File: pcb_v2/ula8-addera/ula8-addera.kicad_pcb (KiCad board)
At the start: 2 copper layers, 54.4 x 61 mm, 13 parts, among them J1 ula8a, U1 74LS283, U2 74LS283, U3 74LS244, U4 74LS125

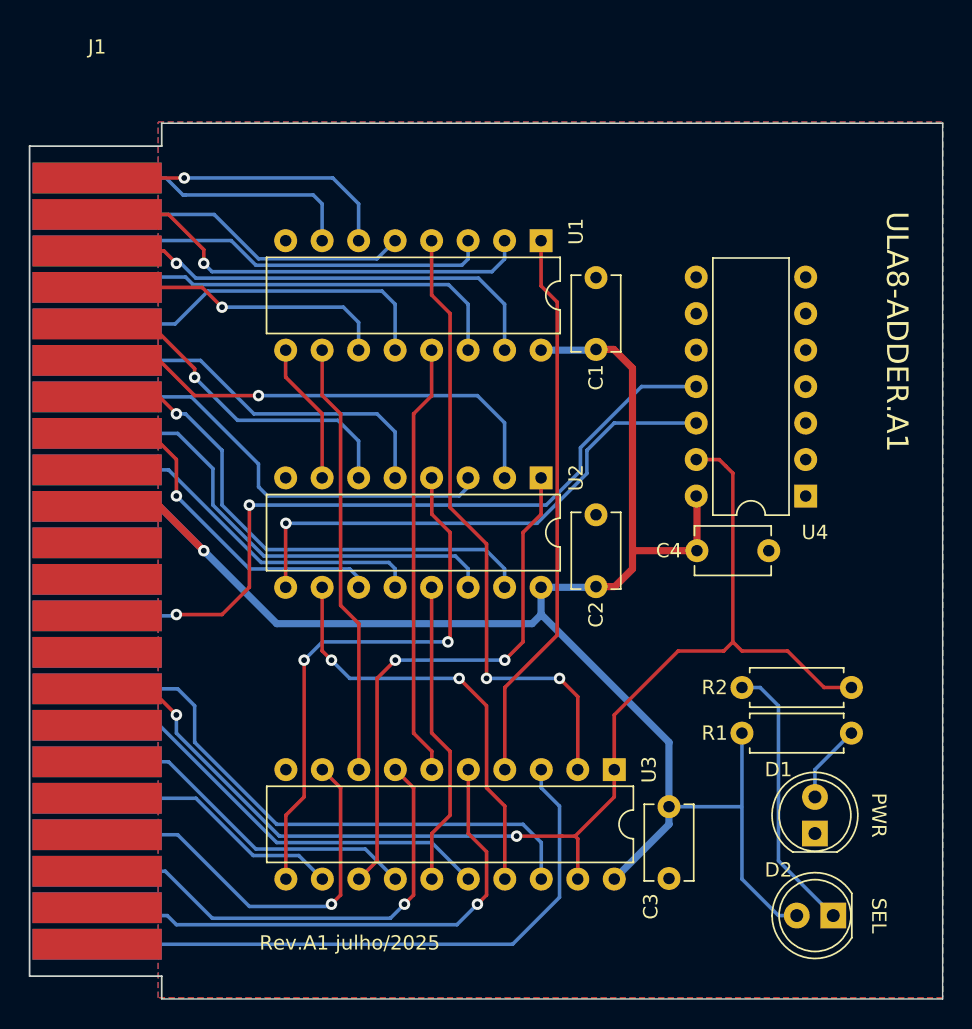
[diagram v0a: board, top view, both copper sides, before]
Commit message: vias de alimentacao movidas para as extremidades do conector
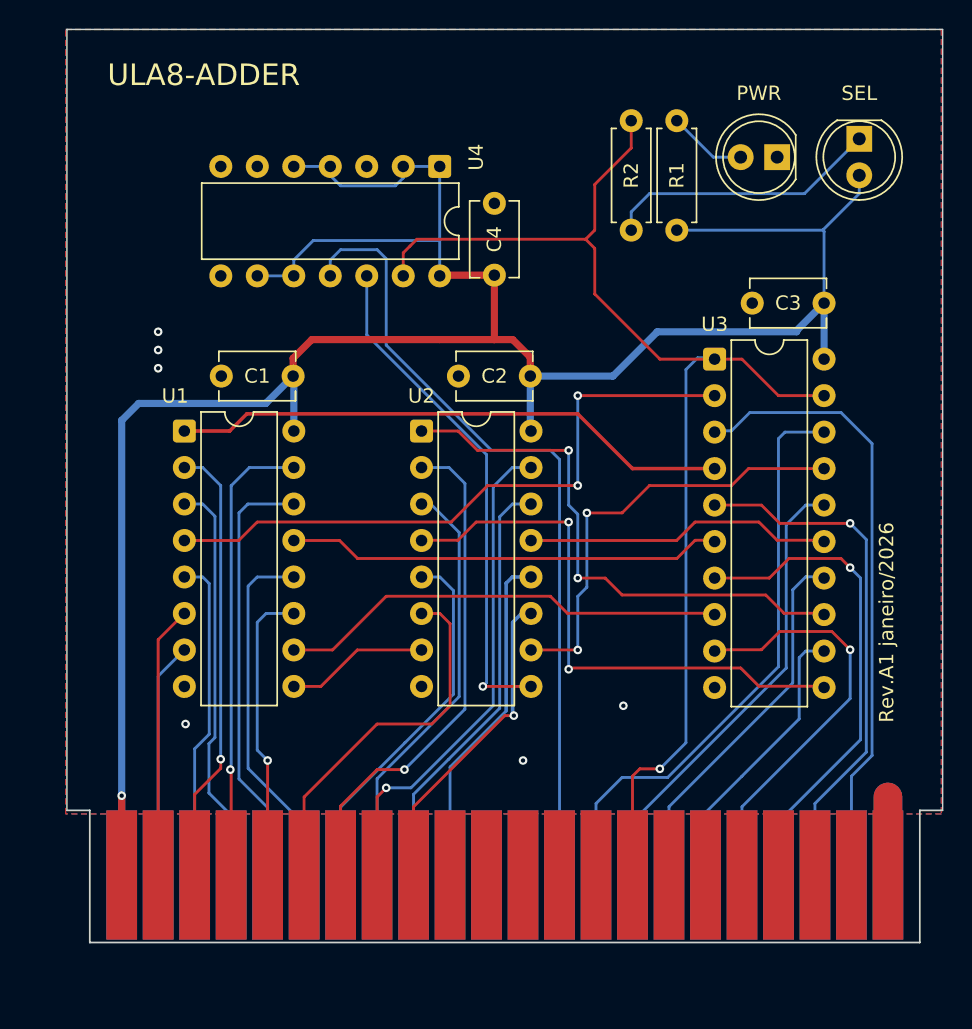
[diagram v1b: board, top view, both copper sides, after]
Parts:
- moved D2 54.1 mm to (83.1, 27.2), turned to -90 degrees
- moved J1 48.6 mm to (31.8, 78.5), turned to 90 degrees
- moved D1 47.2 mm to (77.4, 28.5), turned to 180 degrees
- moved C3 40.5 mm to (75.6, 38.6), turned to 0 degrees
- moved R1 35.3 mm to (70.4, 33.6), turned to 90 degrees
- moved U4 34.3 mm to (53.9, 29.1), turned to -90 degrees
- moved R2 32.8 mm to (67.2, 33.6), turned to 90 degrees
- moved U3 29.4 mm to (73.0, 42.5), turned to 0 degrees
- moved U1 28.1 mm to (36.1, 47.5), turned to 0 degrees
- moved C1 27.0 mm to (38.7, 43.7), turned to 0 degrees
- moved C4 23.8 mm to (57.7, 36.7), turned to 90 degrees
- moved C2 13.6 mm to (55.2, 43.7), turned to 0 degrees
- moved U2 8.94 mm to (52.6, 47.5), turned to 0 degrees
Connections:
- net n_select renamed ~{select}
- J1 pad 1: lower_bus0 -> +5V
- J1 pad 10: +5V -> unconnected-(J1-Pin_10-Pad10)
- J1 pad 11: GND -> unconnected-(J1-Pin_11-Pad11)
- J1 pad 2: lower_bus1 -> lower_bus0
- J1 pad 22: unconnected-(J1-Pad22) -> GND
- J1 pad 23: carry_in -> +5V
- J1 pad 24: upper_bus0 -> carry_in
- J1 pad 25: upper_bus1 -> upper_bus0
- J1 pad 26: upper_bus2 -> upper_bus1
- J1 pad 27: upper_bus3 -> upper_bus2
- J1 pad 28: upper_bus4 -> upper_bus3
- J1 pad 29: upper_bus5 -> upper_bus4
- J1 pad 3: lower_bus2 -> lower_bus1
- J1 pad 30: upper_bus6 -> upper_bus5
- J1 pad 31: upper_bus7 -> upper_bus6
- J1 pad 32: +5V -> upper_bus7
- J1 pad 33: GND -> unconnected-(J1-Pin_33-Pad33)
- J1 pad 36: unconnected-(J1-Pad36) -> ula_bus0
- J1 pad 37: ula_bus0 -> ula_bus1
- J1 pad 38: ula_bus1 -> ula_bus2
- J1 pad 39: ula_bus2 -> ula_bus3
- J1 pad 4: lower_bus3 -> lower_bus2
- J1 pad 40: ula_bus3 -> ula_bus4
- J1 pad 41: ula_bus4 -> ula_bus5
- J1 pad 42: ula_bus5 -> ula_bus6
- J1 pad 43: ula_bus6 -> ula_bus7
- J1 pad 44: ula_bus7 -> GND
- J1 pad 5: lower_bus4 -> lower_bus3
- J1 pad 6: lower_bus5 -> lower_bus4
- J1 pad 7: lower_bus6 -> lower_bus5
- J1 pad 8: lower_bus7 -> lower_bus6
- J1 pad 9: unconnected-(J1-Pad9) -> lower_bus7
- U4 pad 1: unconnected-(U4-Pad1) -> +5V
- U4 pad 10: unconnected-(U4-Pad10) -> +5V
- U4 pad 2: unconnected-(U4-Pad2) -> +5V
- U4 pad 4: unconnected-(U4-Pad4) -> +5V
- U4 pad 5: unconnected-(U4-Pad5) -> +5V
- U4 pad 9: unconnected-(U4-Pad9) -> +5V
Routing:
- net +5V: track 125.0 -> 167.2 mm
- net GND: track 0.00 -> 10.9 mm, vias 0 -> 6
- net carry_out: track 52.6 -> 55.9 mm, vias 2 -> 0
- net lower_bus0: track 21.5 -> 19.0 mm, vias 1 -> 0
- net carry_in: track 19.0 -> 16.4 mm
- net upper_bus6: track 32.5 -> 30.0 mm
- net lower_bus6: track 36.8 -> 34.6 mm
- net lower_bus7: track 24.5 -> 22.4 mm
- net ula_bus2: track 24.1 -> 25.9 mm
- net lower_bus4: track 24.5 -> 26.2 mm, vias 1 -> 0
- net ula_bus3: track 18.0 -> 19.7 mm
- net ula_bus1: track 30.3 -> 31.8 mm
- net lower_bus5: track 34.0 -> 35.4 mm
- net Net-(U2-C4): track 36.9 -> 35.5 mm
- net ula_bus6: track 37.7 -> 36.4 mm
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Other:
- board size 54.4 x 61 mm -> 61 x 54.4 mm
- board text added: "Rev.A1 janeiro/2026"
- board text added: "ULA8-ADDER"
- board text removed: "Rev.A1 julho/2025"
- board text removed: "ULA8-ADDER.A1"

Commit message: revisao completa; mgrfa agora inclui sr8 e sgrda; remover estes dois no proximo commit
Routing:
- net ula_bus4: track 29.4 -> 32.7 mm
- net ula_bus3: track 19.7 -> 22.1 mm
- net ula_bus2: track 25.9 -> 28.3 mm
- net ula_bus5: track 34.5 -> 36.7 mm
- net ula_bus1: track 31.8 -> 34.1 mm
- net ula_bus0: track 40.7 -> 42.6 mm
- net Net-(U1-S1): track 44.7 -> 42.8 mm
- net ula_bus6: track 36.4 -> 37.9 mm
- net ula_bus7: track 43.9 -> 43.1 mm
